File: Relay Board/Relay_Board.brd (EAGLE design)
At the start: 57 x 41 mm, 45 parts, among them J1 22-05-7048-04, J2 22-05-7028-02, J3 22-05-7028-02, K1 G6K-2G-Y, K2 G6K-2G-Y, K3 G6K-2G-Y, K4 G6K-2G-Y, T1 EXMACHINA-LOGO-NAME, U10 SN74LVC2G17DBVR, U9 SN74LVC2G17DBVR, X1 MSTBA2, X12 22-05-7028-02, X13 22-05-7028-02, X14 22-05-7038-03, X15 22-05-7038-03

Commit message: Add free-wheel diode on the schematic and re-route the board
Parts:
- added D1, D2, D3, D4: STPS3L40UF, diode:SMB
- moved T1 78.5 mm to (38.1, 9.53)
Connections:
- net GND: now also D1.A, D2.A, D3.A, D4.A
- net N$24: now also D1.C
- net N$28: now also D3.C
- net N$33: now also D4.C
- net N$55: now also D2.C
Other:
- board text added: "Relay Proto Board Rev A1"
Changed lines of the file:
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@@
 <layer number="24" name="bOrigins" color="15" fill="1" visible="yes" active="yes"/>
 <layer number="25" name="tNames" color="7" fill="1" visible="yes" active="yes"/>
-<layer number="26" name="bNames" color="7" fill="1" visible="no" active="yes"/>
+<layer number="26" name="bNames" color="7" fill="1" visible="yes" active="yes"/>
 <layer number="27" name="tValues" color="7" fill="1" visible="yes" active="yes"/>
-<layer number="28" name="bValues" color="7" fill="1" visible="no" active="yes"/>
+<layer number="28" name="bValues" color="7" fill="1" visible="yes" active="yes"/>
 <layer number="29" name="tStop" color="7" fill="3" visible="no" active="yes"/>
 <layer number="30" name="bStop" color="7" fill="6" visible="no" active="yes"/>
@@
 <wire x1="53" y1="41" x2="4" y2="41" width="0" layer="20"/>
 <wire x1="4" y1="41" x2="0" y2="37" width="0" layer="20" curve="90"/>
+<text x="41.91" y="7.62" size="1.016" layer="21" font="vector">Relay Proto Board
+Rev A1</text>
 </plain>
 <attributes>
@@
 <attribute name="MPN" value="1757242" x="1.905" y="20.5" size="1.778" layer="27" rot="R270" display="off"/>
 </element>
-<element name="T1" library="exmachina" package="EXM-LOGO-BASELINE" value="EXMACHINA-LOGO-NAME" x="-1.27" y="77.47"/>
+<element name="T1" library="exmachina" package="EXM-LOGO-BASELINE" value="EXMACHINA-LOGO-NAME" x="38.1" y="9.525"/>
 <element name="H1" library="holes" package="3,0" value="MOUNT-HOLE3.0" x="4" y="4" locked="yes"/>
 <element name="H2" library="holes" package="3,0" value="MOUNT-HOLE3.0" x="4" y="37" locked="yes"/>
 <element name="H3" library="holes" package="3,0" value="MOUNT-HOLE3.0" x="53" y="4" locked="yes"/>
 <element name="H4" library="holes" package="3,0" value="MOUNT-HOLE3.0" x="53" y="37" locked="yes"/>
+<element name="D1" library="diode" package="SMB" value="STPS3L40UF" x="3.81" y="-19.05">
+<attribute name="OC_FARNELL" value="2341599" x="3.81" y="-19.05" size="1.016" layer="27" font="vector" display="off"/>
+<attribute name="MP" value="STMICROELECTRONICS" x="3.81" y="-19.05" size="1.016" layer="27" font="vector" display="off"/>
+<attribute name="MPN" value="STPS3L40UF" x="3.81" y="-19.05" size="1.016" layer="27" font="vector" display="off"/>
+</element>
+<element name="D2" library="diode" package="SMB" value="STPS3L40UF" x="3.81" y="-25.4">
+<attribute name="OC_FARNELL" value="2341599" x="3.81" y="-25.4" size="1.016" layer="27" font="vector" display="off"/>
+<attribute name="MP" value="STMICROELECTRONICS" x="3.81" y="-25.4" size="1.016" layer="27" font="vector" display="off"/>
+<attribute name="MPN" value="STPS3L40UF" x="3.81" y="-25.4" size="1.016" layer="27" font="vector" display="off"/>
+</element>
+<element name="D3" library="diode" package="SMB" value="STPS3L40UF" x="3.81" y="-31.75">
+<attribute name="OC_FARNELL" value="2341599" x="3.81" y="-31.75" size="1.016" layer="27" font="vector" display="off"/>
+<attribute name="MP" value="STMICROELECTRONICS" x="3.81" y="-31.75" size="1.016" layer="27" font="vector" display="off"/>
+<attribute name="MPN" value="STPS3L40UF" x="3.81" y="-31.75" size="1.016" layer="27" font="vector" display="off"/>
+</element>
+<element name="D4" library="diode" package="SMB" value="STPS3L40UF" x="3.81" y="-38.1">
+<attribute name="OC_FARNELL" value="2341599" x="3.81" y="-38.1" size="1.016" layer="27" font="vector" display="off"/>
+<attribute name="MP" value="STMICROELECTRONICS" x="3.81" y="-38.1" size="1.016" layer="27" font="vector" display="off"/>
+<attribute name="MPN" value="STPS3L40UF" x="3.81" y="-38.1" size="1.016" layer="27" font="vector" display="off"/>
+</element>
 </elements>
 <signals>
@@
 <vertex x="-2.54" y="-7.62"/>
 </polygon>
+<contactref element="D1" pad="A"/>
+<contactref element="D2" pad="A"/>
+<contactref element="D3" pad="A"/>
+<contactref element="D4" pad="A"/>
+<wire x1="6.01" y1="-31.75" x2="6.01" y2="-38.1" width="0" layer="19" extent="1-1"/>
+<wire x1="6.01" y1="-25.4" x2="6.01" y2="-31.75" width="0" layer="19" extent="1-1"/>
+<wire x1="6.01" y1="-19.05" x2="6.01" y2="-25.4" width="0" layer="19" extent="1-1"/>
+<wire x1="22.225" y1="10.375" x2="6.01" y2="-19.05" width="0" layer="19" extent="1-1"/>
 </signal>
 <signal name="+3V3" class="2">
@@
 <wire x1="43.815" y1="27.305" x2="44.45" y2="27.94" width="0.3048" layer="1"/>
 <wire x1="44.45" y1="27.94" x2="44.45" y2="30.9" width="0.3048" layer="1"/>
+<contactref element="D1" pad="C"/>
+<wire x1="1.61" y1="-19.05" x2="41.6" y2="27.295" width="0" layer="19" extent="1-1"/>
 </signal>
 <signal name="N$32">
@@
 <wire x1="33.655" y1="27.305" x2="34.29" y2="27.94" width="0.3048" layer="1"/>
 <wire x1="34.29" y1="27.94" x2="34.29" y2="30.9" width="0.3048" layer="1"/>
+<contactref element="D2" pad="C"/>
+<wire x1="1.61" y1="-25.4" x2="30.805" y2="27.295" width="0" layer="19" extent="1-1"/>
 </signal>
 <signal name="N$57">
@@
 <wire x1="20.655" y1="27.305" x2="24.25" y2="30.9" width="0.3048" layer="1"/>
 <wire x1="24.25" y1="30.9" x2="25.4" y2="30.9" width="0.3048" layer="1"/>
+<contactref element="D3" pad="C"/>
+<wire x1="1.61" y1="-31.75" x2="20.645" y2="27.295" width="0" layer="19" extent="1-1"/>
 </signal>
 <signal name="N$59">
@@
 <wire x1="11.12" y1="27.295" x2="14.725" y2="30.9" width="0.3048" layer="1"/>
 <wire x1="14.725" y1="30.9" x2="16.51" y2="30.9" width="0.3048" layer="1"/>
+<contactref element="D4" pad="C"/>
+<wire x1="11.12" y1="27.295" x2="1.61" y2="-38.1" width="0" layer="19" extent="1-1"/>
 </signal>
 <signal name="N$70">
@@
 </board>
 </drawing>
+<compatibility>
+<note version="6.3" minversion="6.2.2" severity="warning">
+Since Version 6.2.2 text objects can contain more than one line,
+which will not be processed correctly with this version.
+</note>
+</compatibility>
 </eagle>

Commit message: Add fiducial to the board
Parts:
- added JP1, JP2, JP3, JP4: FIDUCIAL1X2, SparkFun:FIDUCIAL-1X2
- R46, R48: value 4k7 -> 4K7
- moved D4 70.9 mm to (11.4, 32.4), turned to 90 degrees
- moved D3 66.4 mm to (21.0, 32.4), turned to 90 degrees
- moved D2 63.4 mm to (29.8, 32.4), turned to 90 degrees
- moved D1 62.9 mm to (40.0, 32.4), turned to 90 degrees
- moved X12 1.91 mm to (26.0, 35.6)
- moved R111 0.64 mm to (26.0, 31.8)
- moved X13 0.63 mm to (15.9, 35.6)
- moved R108 0.63 mm to (34.9, 31.8)
- moved R109 0.63 mm to (45.1, 31.8)
- moved R110 0.63 mm to (17.1, 31.8)
- moved X14 0.63 mm to (45.1, 35.6)
- moved X15 0.63 mm to (34.9, 35.6)
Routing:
- net N$28: track 6.25 -> 9.15 mm
- net N$24: track 6.08 -> 8.94 mm
- net +24V: track 57.6 -> 60.2 mm
- net N$33: track 6.88 -> 9.03 mm
- net N$55: track 6.71 -> 8.68 mm
- net N$32: track 2.96 -> 3.61 mm

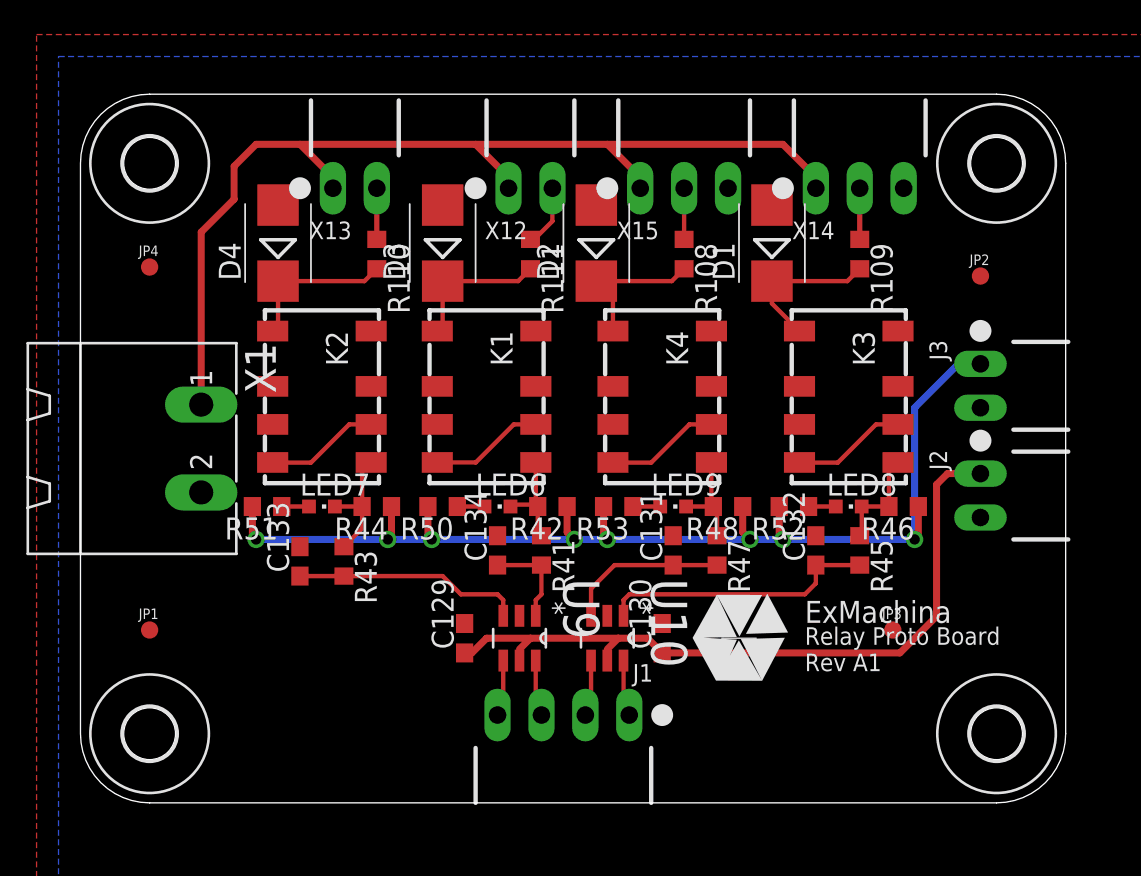
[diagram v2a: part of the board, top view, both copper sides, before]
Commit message: Change name and value size on the board
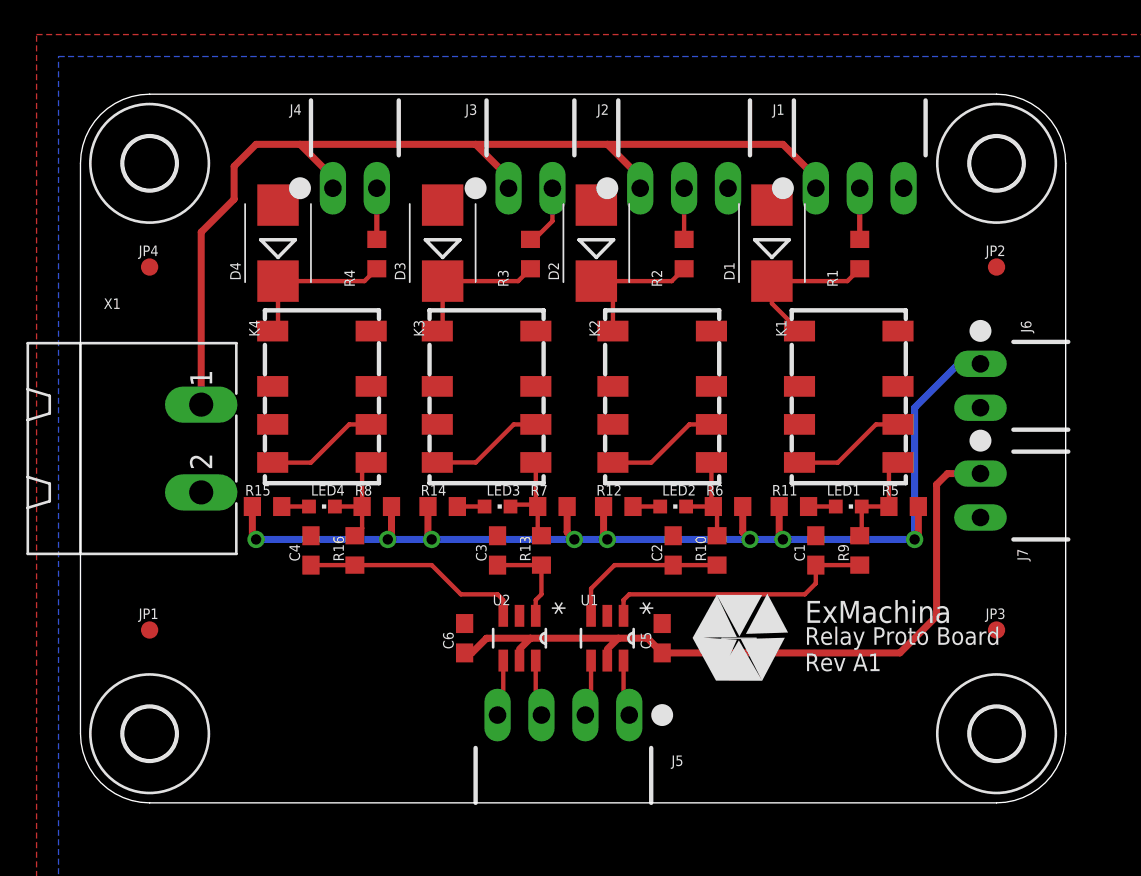
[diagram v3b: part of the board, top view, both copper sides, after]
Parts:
- removed C133: 0.1uF, rcl:C0603
- removed R43: 100, rcl:R0603
- removed X12: 22-05-7028-02, con-molex:7395-02
- removed X14, X15: 22-05-7038-03, con-molex:7395-03
- added C4: 0.1uF, rcl:C0603
- added J5: 22-05-7048-04, con-molex:7395-04
- added J6, J7: 22-05-7028-02, con-molex:7395-02
- added R16: 100, rcl:R0603
- J1: value 22-05-7048-04 -> 22-05-7038-03; device con-molex:7395-04 -> con-molex:7395-03
- J2: value 22-05-7028-02 -> 22-05-7038-03; device con-molex:7395-02 -> con-molex:7395-03
- moved J1 35.0 mm to (45.1, 35.6), turned to 180 degrees
- moved J3 28.4 mm to (26.0, 35.6), turned to 180 degrees
- moved J2 24.7 mm to (34.9, 35.6), turned to 180 degrees
- moved K1 21.0 mm to (44.5, 23.5)
- moved K3 21.0 mm to (23.5, 23.5)
- moved K2 19.7 mm to (33.7, 23.5)
- moved K4 19.7 mm to (14.0, 23.5)
- moved JP3 6.00 mm to (53.0, 10.0)
- moved JP2 1.07 mm to (53.0, 31.0)
- renumbered C129 to C6, C130 to C5, C131 to C2, C132 to C1, C134 to C3, LED6 to LED3, LED7 to LED4, LED8 to LED1, LED9 to LED2, R108 to R2, R109 to R1, R110 to R4, R111 to R3, R41 to R13, R42 to R7, R44 to R8, R45 to R9, R46 to R5, R47 to R10, R48 to R6, R50 to R14, R51 to R15, R52 to R11, R53 to R12, U10 to U1, U9 to U2, X13 to J4
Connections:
- net +24V: now also J1.1, J2.1, J3.1; no longer X12.1, X14.1, X15.1
- net +3V3: now also J7.1; no longer J2.1
- net +5V: now also J6.1; no longer J3.1
- net BRAKE_SENSOR_1: now also J5.1; no longer J1.1
- net BRAKE_SENSOR_2: now also J5.2; no longer J1.2
- net DRIVE_EN: now also J5.3; no longer J1.3
- net DRIVE_ERR: now also J5.4; no longer J1.4
- net GND: now also C4.2, J1.3, J2.3, J6.2, J7.2; no longer C133.2, J2.2, J3.2, X14.3, X15.3
- net N$21: now also J1.2; no longer X14.2
- net N$23: now also J2.2; no longer X15.2
- net N$24: now also K1.1; no longer K3.1
- net N$28: now also K3.1; no longer K1.1
- net N$32: now also J3.2; no longer X12.2
- net N$33: now also K4.1; no longer K2.1
- net N$42: now also C4.1, R16.2; no longer C133.1, R43.2
- net N$55: now also K2.1; no longer K4.1
- net N$58: now also K1.5; no longer K3.5
- net N$71: now also K2.5; no longer K4.5
- net N$73: now also K3.5; no longer K1.5
- net N$75: now also K4.5, R16.1; no longer K2.5, R43.1
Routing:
- net N$75: track 7.10 -> 6.21 mm
